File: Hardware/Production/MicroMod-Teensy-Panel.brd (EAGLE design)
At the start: 177.1 x 83.1 mm, 986 parts, among them J1 MICROMOD-2222, J10 MICROMOD-2222, J11 MICROMOD-2222, J12 MICROMOD-2222, J13 MICROMOD-2222, J14 MICROMOD-2222, J2 MICROMOD-2222, J3 MICROMOD-2222, J4 MICROMOD-2222, J5 MICROMOD-2222, J6 MICROMOD-2222, J7 MICROMOD-2222, J8 MICROMOD-2222, J9 MICROMOD-2222, U1 IMXRT1062DV10X10, U10 IMXRT1062DV10X10, U11 W25QXX, U12 MKL02Z32VFG4, U13 IMXRT1062DV10X10, U14 W25QXX, U15 MKL02Z32VFG4, U16 IMXRT1062DV10X10, U17 W25QXX, U18 MKL02Z32VFG4, U19 IMXRT1062DV10X10, U2 W25QXX, U20 W25QXX, U21 MKL02Z32VFG4, U22 IMXRT1062DV10X10, U23 W25QXX, U24 MKL02Z32VFG4, U25 IMXRT1062DV10X10, U26 W25QXX, U27 MKL02Z32VFG4, U28 IMXRT1062DV10X10, U29 W25QXX, U3 MKL02Z32VFG4, U30 MKL02Z32VFG4, U31 IMXRT1062DV10X10, U32 W25QXX, U33 MKL02Z32VFG4, U34 IMXRT1062DV10X10, U35 W25QXX, U36 MKL02Z32VFG4, U37 IMXRT1062DV10X10, U38 W25QXX, U39 MKL02Z32VFG4, U4 IMXRT1062DV10X10, U40 IMXRT1062DV10X10, U41 W25QXX, U42 MKL02Z32VFG4, U5 W25QXX, U6 MKL02Z32VFG4, U7 IMXRT1062DV10X10, U8 W25QXX, U9 MKL02Z32VFG4, Y1 32.768kHz, Y10 24MHz, Y11 32.768kHz, Y12 24MHz, Y13 32.768kHz, Y14 24MHz, Y15 32.768kHz, Y16 24MHz, Y17 32.768kHz, Y18 24MHz, Y19 32.768kHz, Y2 24MHz, Y20 24MHz, Y21 32.768kHz, Y22 24MHz, Y23 32.768kHz, Y24 24MHz, Y25 32.768kHz, Y26 24MHz, Y27 32.768kHz, Y28 24MHz, Y3 32.768kHz, Y4 24MHz, Y5 32.768kHz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

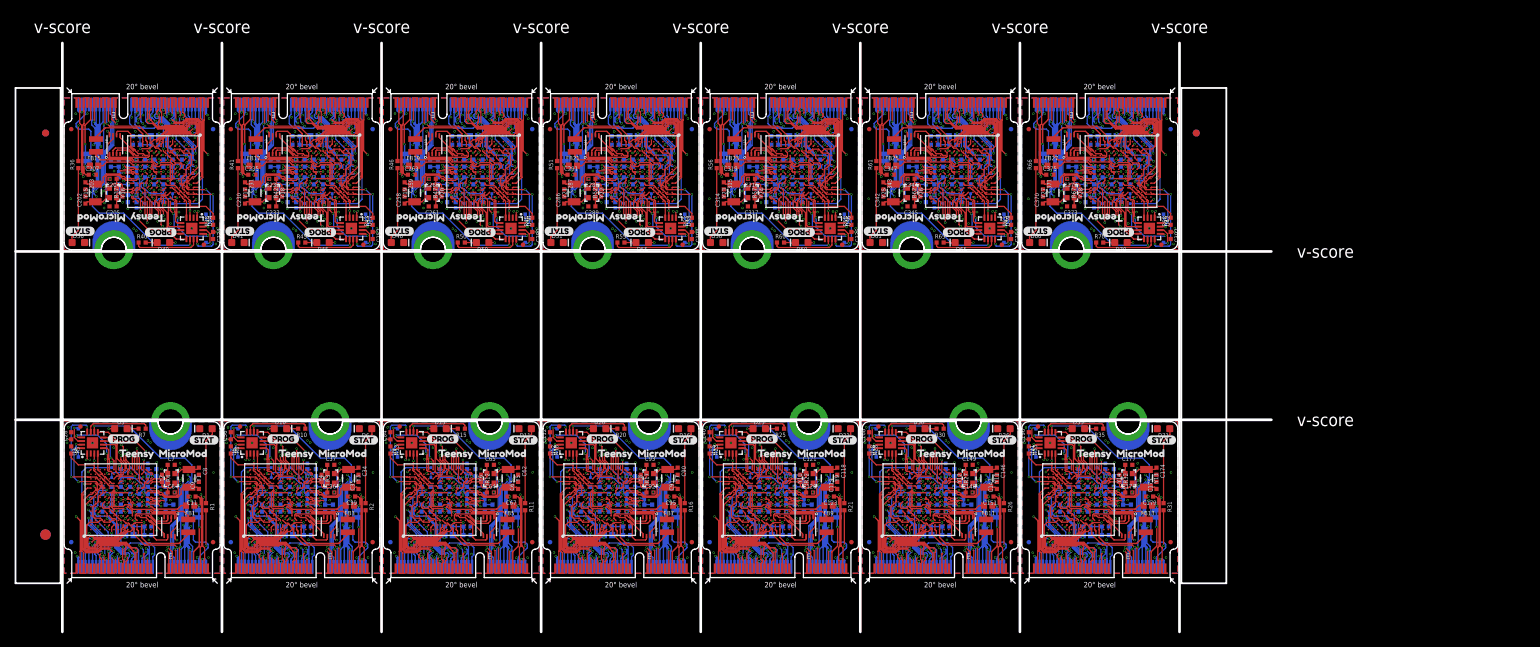
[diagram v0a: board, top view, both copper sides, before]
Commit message: Routed with 5mil. Increased clk spacing.
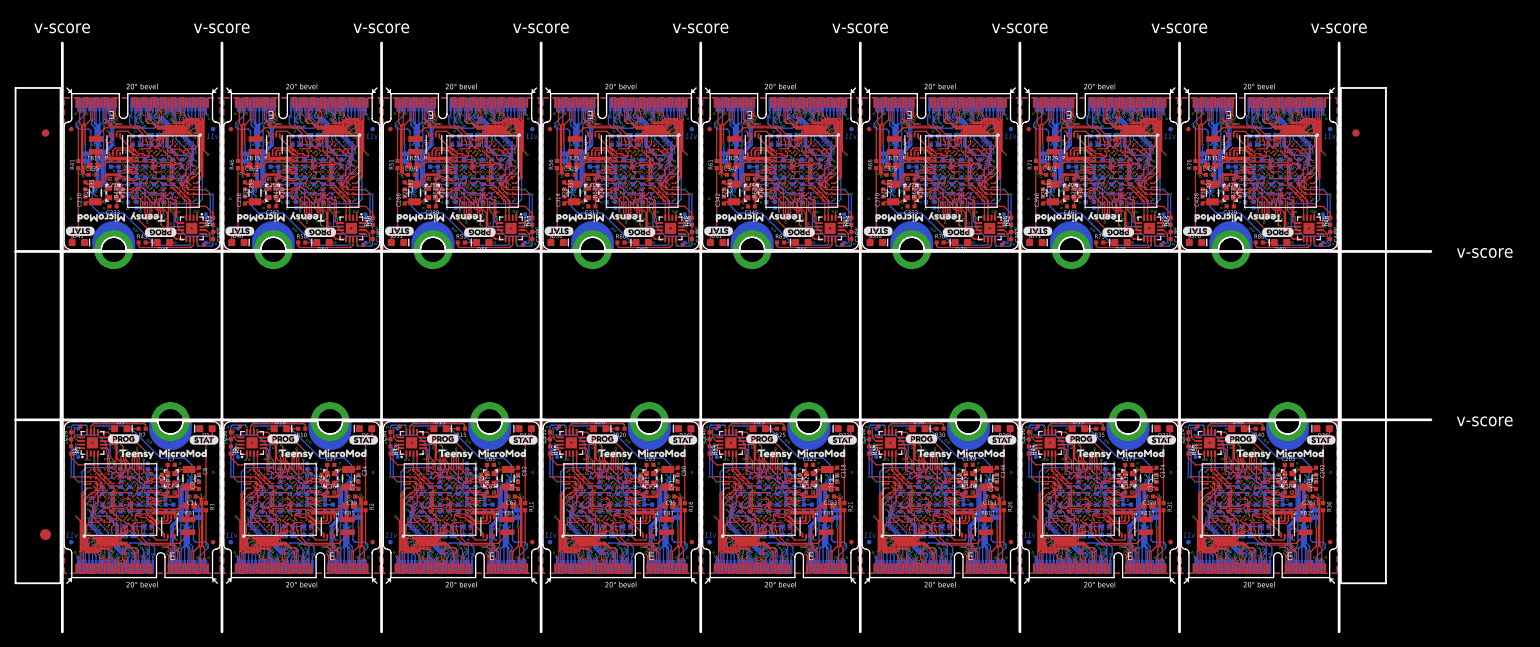
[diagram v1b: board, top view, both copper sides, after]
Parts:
- added C393, C403, C421, C431: 2.2uF, SparkFun-Capacitors:0402-TIGHT
- added C394, C406, C410, C418, C419, C422, C434, C438, C446, C447: 4.7uF, SparkFun-Capacitors:0402-TIGHT
- added C395, C396, C404, C405, C407, C409, C412, C414, C415, C416, C417, C420, C423, C424, C432, C433, C435, C437, C440, C442, C443, C444, C445, C448: 0.22uF, SparkFun-Capacitors:0402-TIGHT
- added C397, C408, C425, C436: 10nF, SparkFun-Capacitors:0402-TIGHT
- added C398, C399, C426, C427: 20pF, SparkFun-Capacitors:0402-TIGHT
- added C400, C401, C428, C429: 12pF, SparkFun-Capacitors:0402-TIGHT
- added C402, C411, C413, C430, C439, C441: 10uF, SparkFun-Capacitors:0402-TIGHT
- added D71, D76: BLUE, SparkFun-LED:LED-0603
- added D72, D77: 120mA370mV, SparkFun-DiscreteSemi:SOD-523
- added D73, D74, D78, D79: 120mA/370mV, SparkFun-DiscreteSemi:SOD-523
- added D75, D80: Yellow, SparkFun-LED:LED-0603
- added FB29, FB30, FB31, FB32: 120Ω, SparkFun-Coils:0402
- added FD57, FD58, FD59, FD60, FD61, FD62, FD63, FD64: FIDUCIALUFIDUCIAL, SparkFun-Aesthetics:FIDUCIAL-MICRO
- added J15, J16: MICROMOD-2222, Teensy:M.2-CARD-E-22
- added L15, L16: 4.7μH, SparkFun-Coils:1008(2520)
- added LOGO15, LOGO16: SFE_LOGO_NAME_FLAME.1_INCH, SparkFun-Aesthetics:SFE_LOGO_NAME_FLAME_.1
- added MEAS14, MEAS15: JUMPER-SMT_2_NC_TRACE_SILK, SparkFun-Jumpers:SMT-JUMPER_2_NC_TRACE_SILK
- added R71, R75, R76, R80: 1k, SparkFun-Resistors:0402-TIGHT
- added R72, R77: 2.2M, SparkFun-Resistors:0402-TIGHT
- added R73, R74, R78, R79: 100k, SparkFun-Resistors:0402-TIGHT
- added TP141, TP151: 32kHz Test, SparkFun-Connectors:PAD.02X.02
- added TP142, TP143, TP144, TP145, TP146, TP147, TP148, TP149, TP150, TP152, TP153, TP154, TP155, TP156, TP157, TP158, TP159, TP160: (no value), SparkFun-Connectors:PAD.02X.02
- added U$100, U$103, U$107, U$110: (no value), buzzard_labels (1):TEENSY2
- added U$101, U$108: (no value), SparkFun-Buzzard:STAT_32
- added U$102, U$109: (no value), SparkFun-Buzzard:PROG_32
- added U$104, U$106, U$111, U$99: (no value), buzzard_labels (1):MICROMOD0
- added U$105, U$112: (no value), SparkFun-Buzzard:MEAS_32
- added U43, U46: IMXRT1062DV10X10, Teensy:IMXRT1062
- added U44, U47: W25QXX3X2, Teensy:USON-8
- added U45, U48: MKL02Z32VFG4, Teensy:QFN-16
- added Y29, Y31: 32.768kHz, SparkFun-Clocks:CRYSTAL-SMD-3.2X1.5MM
- added Y30, Y32: 24MHz, SparkFun-Clocks:CRYSTAL-SMD-2.0X1.6MM
- MEAS, MEAS1, MEAS10, MEAS11, MEAS12, MEAS13, MEAS2, MEAS3, MEAS4, MEAS5, MEAS6, MEAS7, MEAS8, MEAS9: value (none) -> JUMPER-SMT_2_NC_TRACE_SILK
- U11, U14, U17, U2, U20, U23, U26, U29, U32, U35, U38, U41, U5, U8: value W25QXX -> W25QXX3X2
- moved FD29 186.9 mm to (178.6, 5.80), turned to 0 degrees
- moved U$56 186.1 mm to (178.7, 7.40), turned to 90 degrees
- moved U$55 182.6 mm to (179.2, 16.3), turned to 0 degrees
- moved R36 182.1 mm to (177.6, 10.8), turned to 270 degrees
- moved MEAS7 180.7 mm to (176.6, 9.80), turned to 90 degrees
- moved U$54 179.8 mm to (178.1, 17.9), turned to 0 degrees
- moved FD32 179.5 mm to (178.6, 21.8), turned to 0 degrees
- moved L8 178.8 mm to (175.1, 8.10), turned to 90 degrees
- moved C203 178.6 mm to (176.6, 13.8), turned to 90 degrees
- moved C202 177.7 mm to (176.6, 15.8), turned to 270 degrees
- moved FB15 177.7 mm to (175.3, 11.0), turned to 180 degrees
- moved C207 177.5 mm to (175.6, 12.2), turned to 180 degrees
- moved D36 177.5 mm to (177.6, 21.8), turned to 180 degrees
- moved Y15 175.4 mm to (175.2, 14.8), turned to 270 degrees
- moved U23 173.8 mm to (172.4, 7.99), turned to 270 degrees
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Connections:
- net ADC1ST/14/A0 renamed A0/14
- net ADC1ST/14/A1 renamed A0/1
- net ADC1ST/14/A10 renamed A0/10
- net ADC1ST/14/A11 renamed A0/11
- net ADC1ST/14/A12 renamed A0/12
- net ADC1ST/14/A13 renamed A0/13
- net ADC1ST/14/A2 renamed A0/2
- net ADC1ST/14/A3 renamed A0/3
- net ADC1ST/14/A4 renamed A0/4
- net ADC1ST/14/A5 renamed A0/5
- net ADC1ST/14/A6 renamed A0/6
- net ADC1ST/14/A7 renamed A0/7
- net ADC1ST/14/A8 renamed A0/8
- net ADC1ST/14/A9 renamed A0/9
- net ADC2ND/15/A1 renamed A1/15
- net ADC2ND/15/A10 renamed A1/9
- net ADC2ND/15/A11 renamed A1/10
- net ADC2ND/15/A12 renamed A1/11
- net ADC2ND/15/A13 renamed A1/12
- net ADC2ND/15/A14 renamed A1/13
- net ADC2ND/15/A2 renamed A1/1
- net ADC2ND/15/A3 renamed A1/2
- net ADC2ND/15/A4 renamed A1/3
- net ADC2ND/15/A5 renamed A1/4
- net ADC2ND/15/A6 renamed A1/5
- net ADC2ND/15/A7 renamed A1/6
- net ADC2ND/15/A8 renamed A1/7
- net ADC2ND/15/A9 renamed A1/8
- net GPIO_1ST/1 renamed D0/1
- net GPIO_1ST/10 renamed D0/10
- net GPIO_1ST/11 renamed D0/11
- net GPIO_1ST/12 renamed D0/12
- net GPIO_1ST/13 renamed D0/13
- net GPIO_1ST/14 renamed D0/14
- net GPIO_1ST/2 renamed D0/2
- net GPIO_1ST/3 renamed D0/3
- net GPIO_1ST/4 renamed D0/4
- net GPIO_1ST/5 renamed D0/5
- net GPIO_1ST/6 renamed D0/6
- net GPIO_1ST/7 renamed D0/7
- net GPIO_1ST/8 renamed D0/8
- net GPIO_1ST/9 renamed D0/9
- net GPIO_2ND/1 renamed D1/1
- net GPIO_2ND/10 renamed D1/10
- net GPIO_2ND/11 renamed D1/11
- net GPIO_2ND/12 renamed D1/12
- net GPIO_2ND/13 renamed D1/13
- net GPIO_2ND/14 renamed D1/14
- net GPIO_2ND/2 renamed D1/2
- net GPIO_2ND/3 renamed D1/3
- net GPIO_2ND/4 renamed D1/4
- net GPIO_2ND/5 renamed D1/5
- net GPIO_2ND/6 renamed D1/6
- net GPIO_2ND/7 renamed D1/7
- net GPIO_2ND/8 renamed D1/8
- net GPIO_2ND/9 renamed D1/9
- net PWM_1ST/1 renamed PWM0/1
- net PWM_1ST/10 renamed PWM0/10
- net PWM_1ST/11 renamed PWM0/11
- net PWM_1ST/12 renamed PWM0/12
- net PWM_1ST/13 renamed PWM0/13
- net PWM_1ST/14 renamed PWM0/14
- net PWM_1ST/2 renamed PWM0/2
- net PWM_1ST/3 renamed PWM0/3
- net PWM_1ST/4 renamed PWM0/4
- net PWM_1ST/5 renamed PWM0/5
- net PWM_1ST/6 renamed PWM0/6
- net PWM_1ST/7 renamed PWM0/7
- net PWM_1ST/8 renamed PWM0/8
- net PWM_1ST/9 renamed PWM0/9
- net PWM_2ND/1 renamed PWM1/1
- net PWM_2ND/10 renamed PWM1/10
- net PWM_2ND/11 renamed PWM1/11
- net PWM_2ND/12 renamed PWM1/12
- net PWM_2ND/13 renamed PWM1/13
- net PWM_2ND/14 renamed PWM1/14
- net PWM_2ND/2 renamed PWM1/2
- net PWM_2ND/3 renamed PWM1/3
- net PWM_2ND/4 renamed PWM1/4
- net PWM_2ND/5 renamed PWM1/5
- net PWM_2ND/6 renamed PWM1/6
- net PWM_2ND/7 renamed PWM1/7
- net PWM_2ND/8 renamed PWM1/8
- net PWM_2ND/9 renamed PWM1/9
- net SCL2/24/A1 renamed SCL1/24/A1
- net SCL2/24/A10 renamed SCL1/24/A10
- net SCL2/24/A11 renamed SCL1/24/A11
- net SCL2/24/A12 renamed SCL1/24/A12
- net SCL2/24/A13 renamed SCL1/24/A13
- net SCL2/24/A14 renamed SCL1/24/A14
- net SCL2/24/A2 renamed SCL1/24/A2
- net SCL2/24/A3 renamed SCL1/24/A3
- net SCL2/24/A4 renamed SCL1/24/A4
- net SCL2/24/A5 renamed SCL1/24/A5
- net SCL2/24/A6 renamed SCL1/24/A6
- net SCL2/24/A7 renamed SCL1/24/A7
- net SCL2/24/A8 renamed SCL1/24/A8
- net SCL2/24/A9 renamed SCL1/24/A9
- net SDA2/25/A1 renamed SDA1/25/A1
- net SDA2/25/A10 renamed SDA1/25/A10
- net SDA2/25/A11 renamed SDA1/25/A11
- net SDA2/25/A12 renamed SDA1/25/A12
- net SDA2/25/A13 renamed SDA1/25/A13
- net SDA2/25/A14 renamed SDA1/25/A14
- net SDA2/25/A2 renamed SDA1/25/A2
- net SDA2/25/A3 renamed SDA1/25/A3
- net SDA2/25/A4 renamed SDA1/25/A4
- net SDA2/25/A5 renamed SDA1/25/A5
- net SDA2/25/A6 renamed SDA1/25/A6
- net SDA2/25/A7 renamed SDA1/25/A7
- net SDA2/25/A8 renamed SDA1/25/A8
- net SDA2/25/A9 renamed SDA1/25/A9
- new net 3.3V14: C393.1, C394.1, C395.1, C396.1, C397.1, C420.1, D72.A, D75.A, FB30.1, J15.2, J15.4, J15.74, R74.1, U43.E6, U43.E9, U43.F10, U43.F5, U43.J10, U43.J6, U43.K4, U43.K5, U43.N14, U43.P12, U44.8, U45.1
- new net 3.3V15: C421.1, C422.1, C423.1, C424.1, C425.1, C448.1, D77.A, D80.A, FB32.1, J16.2, J16.4, J16.74, R79.1, U46.E6, U46.E9, U46.F10, U46.F5, U46.J10, U46.J6, U46.K4, U46.K5, U46.N14, U46.P12, U47.8, U48.1
- new net 34/DAT15: J15.66, U43.K1
- new net 34/DAT16: J16.66, U46.K1
- new net 35/DAT14: J15.64, U43.J1
- new net 35/DAT15: J16.64, U46.J1
- new net 36/CLK14: J15.60, U43.J3
- new net 36/CLK15: J16.60, U46.J3
- new net 37/CMD14: J15.62, U43.J4
- new net 37/CMD15: J16.62, U46.J4
- new net 38/DAT15: J15.70, U43.H2
- new net 38/DAT16: J16.70, U46.H2
- new net 39/DAT15: J15.68, U43.J2
- new net 39/DAT16: J16.68, U46.J2
- new net A0/15: J15.34, U43.L11
- new net A0/16: J16.34, U46.L11
- new net A1/14: J15.38, U43.M12
- new net A1/16: J16.38, U46.M12
- new net AUD_IN/15: J15.54, U43.A11
- new net AUD_IN/16: J16.54, U46.A11
- new net AUD_OUT/15: J15.56, U43.B11
- new net AUD_OUT/16: J16.56, U46.B11
- new net BATT_VIN/22/A15: J15.51, U43.H13
- new net BATT_VIN/22/A16: J16.51, U46.H13
- new net BCLK/21/A15: J15.50, U43.J13
- new net BCLK/21/A16: J16.50, U46.J13
- new net BOOTMODE14: U43.F11, U45.4
- new net BOOTMODE15: U46.F11, U48.4
- new net CAN_RX/14: J15.41, U43.E4
- new net CAN_RX/15: J16.41, U46.E4
- new net CAN_TX/14: J15.43, U43.C3
- new net CAN_TX/15: J16.43, U46.C3
- new net CS/15: J15.49, U43.D7
- new net CS/16: J16.49, U46.D7
- new net D0/15: J15.10, U43.H5
- new net D0/16: J16.10, U46.H5
- new net D1/15: J15.18, U43.H3
- new net D1/16: J16.18, U46.H3
- new net DEBUG_EN14: U43.F3, U45.15
- new net DEBUG_EN15: U46.F3, U48.15
- new net DEBUG_SWO14: U43.D10, U45.12
- new net DEBUG_SWO15: U46.D10, U48.12
- new net GND14: C393.2, C394.2, C395.2, C396.2, C397.2, C398.2, C399.2, C400.2, C401.2, C402.2, C403.2, C404.2, C405.2, C406.2, C407.2, C408.2, C409.2, C410.2, C411.2, C412.2, C413.2, C414.2, C415.2, C416.2, C417.2, C418.2, C419.2, C420.2, D71.C, J15.1, J15.33, J15.36, J15.39, J15.45, J15.7, J15.75, J15.GND, J15.GND-SM-B, R72.1, R73.1, U43.A1, U43.A14, U43.B10, U43.B5, U43.E13, U43.E2, U43.G14, U43.G7, U43.G8, U43.H7, U43.H8, U43.J7, U43.J8, U43.K13, U43.K2, U43.K6, U43.K9, U43.L9, U43.N1, U43.N2, U43.N5, U43.N8, U43.P1, U43.P14, U44.4, U45.17, U45.2
- new net GND15: C421.2, C422.2, C423.2, C424.2, C425.2, C426.2, C427.2, C428.2, C429.2, C430.2, C431.2, C432.2, C433.2, C434.2, C435.2, C436.2, C437.2, C438.2, C439.2, C440.2, C441.2, C442.2, C443.2, C444.2, C445.2, C446.2, C447.2, C448.2, D76.C, J16.1, J16.33, J16.36, J16.39, J16.45, J16.7, J16.75, J16.GND, J16.GND-SM-B, R77.1, R78.1, U46.A1, U46.A14, U46.B10, U46.B5, U46.E13, U46.E2, U46.G14, U46.G7, U46.G8, U46.H7, U46.H8, U46.J7, U46.J8, U46.K13, U46.K2, U46.K6, U46.K9, U46.L9, U46.N1, U46.N2, U46.N5, U46.N8, U46.P1, U46.P14, U47.4, U48.17, U48.2
- new net GPIO/26/A15: J15.42, U43.G12
- new net GPIO/26/A16: J16.42, U46.G12
- new net GPIO/27/A15: J15.44, U43.J14
- new net GPIO/27/A16: J16.44, U46.J14
- new net GPIO/71: J15.71, U43.A10
- new net GPIO/72: J15.40, U43.D9
- new net GPIO/73: J15.46, U43.D5
- new net GPIO/74: J15.48, U43.C10
- new net GPIO/75: J15.73, U43.H4
- new net GPIO/76: J16.71, U46.A10
- new net GPIO/77: J16.40, U46.D9
- new net GPIO/78: J16.46, U46.D5
- new net GPIO/79: J16.48, U46.C10
- new net GPIO/80: J16.73, U46.H4
- new net I2C_!INT!/14: J15.16, U43.C5
- new net I2C_!INT!/15: J16.16, U46.C5
- new net JTAG_MOD14: U43.F13, U45.13
- new net JTAG_MOD15: U46.F13, U48.13
- new net JTAG_TCK14: U43.F12, U45.8
- new net JTAG_TCK15: U46.F12, U48.8
- new net JTAG_TDI14: U43.F14, U45.7
- new net JTAG_TDI15: U46.F14, U48.7
- new net JTAG_TDO14: U43.G13, U45.6
- new net JTAG_TDO15: U46.G13, U48.6
- new net JTAG_TMS14: U43.E14, U45.5
- new net JTAG_TMS15: U46.E14, U48.5
- new net JTAG_TRST14: R73.2, U43.G10, U43.K3, U45.3
- new net JTAG_TRST15: R78.2, U46.G10, U46.K3, U48.3
- new net LRCLK/20/A15: J15.52, U43.L13
- new net LRCLK/20/A16: J16.52, U46.L13
- new net MCLK/23/A15: J15.58, U43.M13
- new net MCLK/23/A16: J16.58, U46.M13
- new net MISO/15: J15.61, U43.E7
- new net MISO/16: J16.61, U46.E7
- new net MOSI/15: J15.59, U43.E8
- new net MOSI/16: J16.59, U46.E8
- new net N$197: C399.1, U43.P9, Y29.P$2
- new net N$198: C398.1, U43.N9, Y29.P$1
- new net N$199: TP141.P$1, U43.M14
- new net N$200: D71.A, R71.1
- new net N$201: C401.1, U43.N11, Y30.3
- new net N$202: C400.1, R72.2, U43.P11, Y30.1
- new net N$203: C402.1, C406.1, C407.1, FB30.2, U43.L1, U43.L2
- new net N$204: L15.1, U43.M1, U43.M2
- new net N$205: C415.1, TP144.P$1, U43.M10
- new net N$206: C416.1, C418.1, TP145.P$1, U43.P10
- new net N$207: C417.1, C419.1, TP146.P$1, U43.P8
- new net N$208: R75.1, U45.11
- new net N$209: D75.C, R75.2
- new net N$210: C403.1, FB29.1, MEAS14.2
- new net N$211: C427.1, U46.P9, Y31.P$2
- new net N$212: C426.1, U46.N9, Y31.P$1
- new net N$213: TP151.P$1, U46.M14
- new net N$214: D76.A, R76.1
- new net N$215: C429.1, U46.N11, Y32.3
- new net N$216: C428.1, R77.2, U46.P11, Y32.1
- new net N$217: C430.1, C434.1, C435.1, FB32.2, U46.L1, U46.L2
- new net N$218: L16.1, U46.M1, U46.M2
- new net N$219: C443.1, TP154.P$1, U46.M10
- new net N$220: C444.1, C446.1, TP155.P$1, U46.P10
- new net N$221: C445.1, C447.1, TP156.P$1, U46.P8
- new net N$222: R80.1, U48.11
- new net N$223: D80.C, R80.2
- new net N$224: C431.1, FB31.1, MEAS15.2
- new net ON/!OFF!14: J15.6, U43.M6
- new net ON/!OFF!15: J16.6, U46.M6
- new net PMIC14: R74.2, U43.K7
- new net PMIC15: R79.2, U46.K7
- new net PORB_RESET14: U43.M7, U45.9
- new net PORB_RESET15: U46.M7, U48.9
- new net PROGRAM14: J15.11, U45.10
- new net PROGRAM15: J16.11, U48.10
- new net PWM0/15: J15.32, U43.G5
- new net PWM0/16: J16.32, U46.G5
- new net PWM1/15: J15.47, U43.F2
- new net PWM1/16: J16.47, U46.F2
- new net QSPI-CLK14: U43.L4, U44.6
- new net QSPI-CLK15: U46.L4, U47.6
- new net QSPI-CS14: U43.L3, U44.1
- new net QSPI-CS15: U46.L3, U47.1
- new net QSPI56: U43.P3, U44.5
- new net QSPI57: U43.N4, U44.2
- new net QSPI58: U43.P4, U44.3
- new net QSPI59: U43.P5, U44.7
- new net QSPI60: U46.P3, U47.5
- new net QSPI61: U46.N4, U47.2
- new net QSPI62: U46.P4, U47.3
- new net QSPI63: U46.P5, U47.7
- new net RX0/14: J15.19, U43.G11
- new net RX0/15: J16.19, U46.G11
- new net RX1/16/A15: J15.20, U43.K10
- new net RX1/16/A16: J16.20, U46.K10
- new net SCK/15: J15.57, R71.2, U43.D8
- new net SCK/16: J16.57, R76.2, U46.D8
- new net SCL/19/A15: J15.14, U43.J11
- new net SCL/19/A16: J16.14, U46.J11
- new net SCL1/24/A15: J15.55, U43.K14
- new net SCL1/24/A16: J16.55, U46.K14
- new net SDA/18/A15: J15.12, U43.K11
- new net SDA/18/A16: J16.12, U46.K11
- new net SDA1/25/A15: J15.53, U43.L14
- new net SDA1/25/A16: J16.53, U46.L14
- new net SWD_CLK14: J15.21, TP148.P$1, U45.14
- new net SWD_CLK15: J16.21, TP158.P$1, U48.14
- new net SWD_DIO14: J15.23, TP147.P$1, U45.16
- new net SWD_DIO15: J16.23, TP157.P$1, U48.16
- new net TX0/15: J15.17, U43.M11
- new net TX0/16: J16.17, U46.M11
- new net TX1/17/A15: J15.22, U43.J12
- new net TX1/17/A16: J16.22, U46.J12
- new net USB2_D+14: J15.35, U43.P7
- new net USB2_D+15: J16.35, U46.P7
- new net USB2_D-14: J15.37, U43.N7
- new net USB2_D-15: J16.37, U46.N7
- new net USB_D+14: J15.3, U43.L8
- new net USB_D+15: J16.3, U46.L8
- new net USB_D-14: J15.5, U43.M8
- new net USB_D-15: J16.5, U46.M8
- new net VCC14: C404.1, C405.1, FB29.2, TP142.P$1, U43.N6, U43.P6
- new net VCC15: C432.1, C433.1, FB31.2, TP152.P$1, U46.N6, U46.P6
- new net VDD_SOC_IN14: C408.1, C409.1, C410.1, C411.1, L15.2, TP149.P$1, U43.F6, U43.F7, U43.F8, U43.F9, U43.G6, U43.G9, U43.H6, U43.H9, U43.J5, U43.J9
- new net VDD_SOC_IN15: C436.1, C437.1, C438.1, C439.1, L16.2, TP159.P$1, U46.F6, U46.F7, U46.F8, U46.F9, U46.G6, U46.G9, U46.H6, U46.H9, U46.J5, U46.J9
- new net VDD_USB_CAP14: C412.1, C413.1, D74.A, TP150.P$1, U43.K8
- new net VDD_USB_CAP15: C440.1, C441.1, D79.A, TP160.P$1, U46.K8
- new net VSS_SNVS_IN14: C414.1, D72.C, D73.C, D74.C, TP143.P$1, U43.M9
- new net VSS_SNVS_IN15: C442.1, D77.C, D78.C, D79.C, TP153.P$1, U46.M9
- new net V_BATT14: D73.A, J15.72
- new net V_BATT15: D78.A, J16.72
- new net V_USB14: J15.9, MEAS14.1
- new net V_USB15: J16.9, MEAS15.1
- net RX0/0: now also J1.19; no longer J1.20
- net RX0/1: now also J2.19; no longer J2.20
- net RX0/10: now also J11.19; no longer J11.20
- net RX0/11: now also J12.19; no longer J12.20
- net RX0/12: now also J13.19; no longer J13.20
- net RX0/13: now also J14.19; no longer J14.20
- net RX0/2: now also J3.19; no longer J3.20
- net RX0/3: now also J4.19; no longer J4.20
- net RX0/4: now also J5.19; no longer J5.20
- net RX0/5: now also J6.19; no longer J6.20
- net RX0/6: now also J7.19; no longer J7.20
- net RX0/7: now also J8.19; no longer J8.20
- net RX0/8: now also J9.19; no longer J9.20
- net RX0/9: now also J10.19; no longer J10.20
- net RX1/16/A1: now also J2.20; no longer J2.19
- net RX1/16/A10: now also J10.20; no longer J10.19
- net RX1/16/A11: now also J11.20; no longer J11.19
- net RX1/16/A12: now also J12.20; no longer J12.19
- net RX1/16/A13: now also J13.20; no longer J13.19
- net RX1/16/A14: now also J14.20; no longer J14.19
- net RX1/16/A2: now also J1.20; no longer J1.19
- net RX1/16/A3: now also J3.20; no longer J3.19
- net RX1/16/A4: now also J4.20; no longer J4.19
- net RX1/16/A5: now also J5.20; no longer J5.19
- net RX1/16/A6: now also J6.20; no longer J6.19
- net RX1/16/A7: now also J7.20; no longer J7.19
- net RX1/16/A8: now also J8.20; no longer J8.19
- net RX1/16/A9: now also J9.20; no longer J9.19
- net TX0/1: now also J1.17; no longer J1.22
- net TX0/10: now also J10.17; no longer J10.22
- net TX0/11: now also J11.17; no longer J11.22
- net TX0/12: now also J12.17; no longer J12.22
- net TX0/13: now also J13.17; no longer J13.22
- net TX0/14: now also J14.17; no longer J14.22
- net TX0/2: now also J2.17; no longer J2.22
- net TX0/3: now also J3.17; no longer J3.22
- net TX0/4: now also J4.17; no longer J4.22
- net TX0/5: now also J5.17; no longer J5.22
- net TX0/6: now also J6.17; no longer J6.22
- net TX0/7: now also J7.17; no longer J7.22
- net TX0/8: now also J8.17; no longer J8.22
- net TX0/9: now also J9.17; no longer J9.22
- net TX1/17/A1: now also J2.22; no longer J2.17
- net TX1/17/A10: now also J10.22; no longer J10.17
- net TX1/17/A11: now also J11.22; no longer J11.17
- net TX1/17/A12: now also J12.22; no longer J12.17
- net TX1/17/A13: now also J13.22; no longer J13.17
- net TX1/17/A14: now also J14.22; no longer J14.17
- net TX1/17/A2: now also J3.22; no longer J3.17
- net TX1/17/A3: now also J1.22; no longer J1.17
- net TX1/17/A4: now also J4.22; no longer J4.17
- net TX1/17/A5: now also J5.22; no longer J5.17
- net TX1/17/A6: now also J6.22; no longer J6.17
- net TX1/17/A7: now also J7.22; no longer J7.17
- net TX1/17/A8: now also J8.22; no longer J8.17
- net TX1/17/A9: now also J9.22; no longer J9.17
- net VDD_SOC_IN: now also U1.J5
- net VDD_SOC_IN1: now also U4.J5
- net VDD_SOC_IN10: now also U31.J5
- net VDD_SOC_IN11: now also U34.J5
- net VDD_SOC_IN12: now also U37.J5
- net VDD_SOC_IN13: now also U40.J5
- net VDD_SOC_IN2: now also U7.J5
- net VDD_SOC_IN3: now also U10.J5
- net VDD_SOC_IN4: now also U13.J5
- net VDD_SOC_IN5: now also U16.J5
- net VDD_SOC_IN6: now also U19.J5
- net VDD_SOC_IN7: now also U22.J5
- net VDD_SOC_IN8: now also U25.J5
- net VDD_SOC_IN9: now also U28.J5
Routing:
- net SWD_CLK15: track 0.00 -> 34.9 mm, vias 0 -> 3
- net SWD_CLK14: track 0.00 -> 34.9 mm, vias 0 -> 3
- net SCK/16: track 0.00 -> 34.8 mm, vias 0 -> 4
- net SCK/15: track 0.00 -> 34.8 mm, vias 0 -> 4
- net PROGRAM15: track 0.00 -> 32.0 mm, vias 0 -> 2
- net PROGRAM14: track 0.00 -> 32.0 mm, vias 0 -> 2
- net SWD_DIO15: track 0.00 -> 31.8 mm, vias 0 -> 3
- net SWD_DIO14: track 0.00 -> 31.8 mm, vias 0 -> 3
- net A0/16: track 0.00 -> 29.0 mm, vias 0 -> 2
- net A0/15: track 0.00 -> 29.0 mm, vias 0 -> 2
- net JTAG_TRST15: track 0.00 -> 28.2 mm, vias 0 -> 3
- net JTAG_TRST14: track 0.00 -> 28.2 mm, vias 0 -> 3
- net TX0/16: track 0.00 -> 28.1 mm, vias 0 -> 3
- net TX0/15: track 0.00 -> 28.1 mm, vias 0 -> 3
- net 3.3V15: track 0.00 -> 26.0 mm, vias 0 -> 12
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- added copper zone on layer 2, net 3.3V14
- added copper zone on layer 2, net 3.3V15
- added copper zone on layer 1, net GND14
- added copper zone on layer 15, net GND14
- added copper zone on layer 16, net GND14
- added copper zone on layer 1, net GND15
- added copper zone on layer 15, net GND15
- added copper zone on layer 16, net GND15
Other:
- board size 177.1 x 83.1 mm -> 199.6 x 83.1 mm
- board text added: "v11"

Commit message: Breakout PMIC. Reduce beads to 0402T.
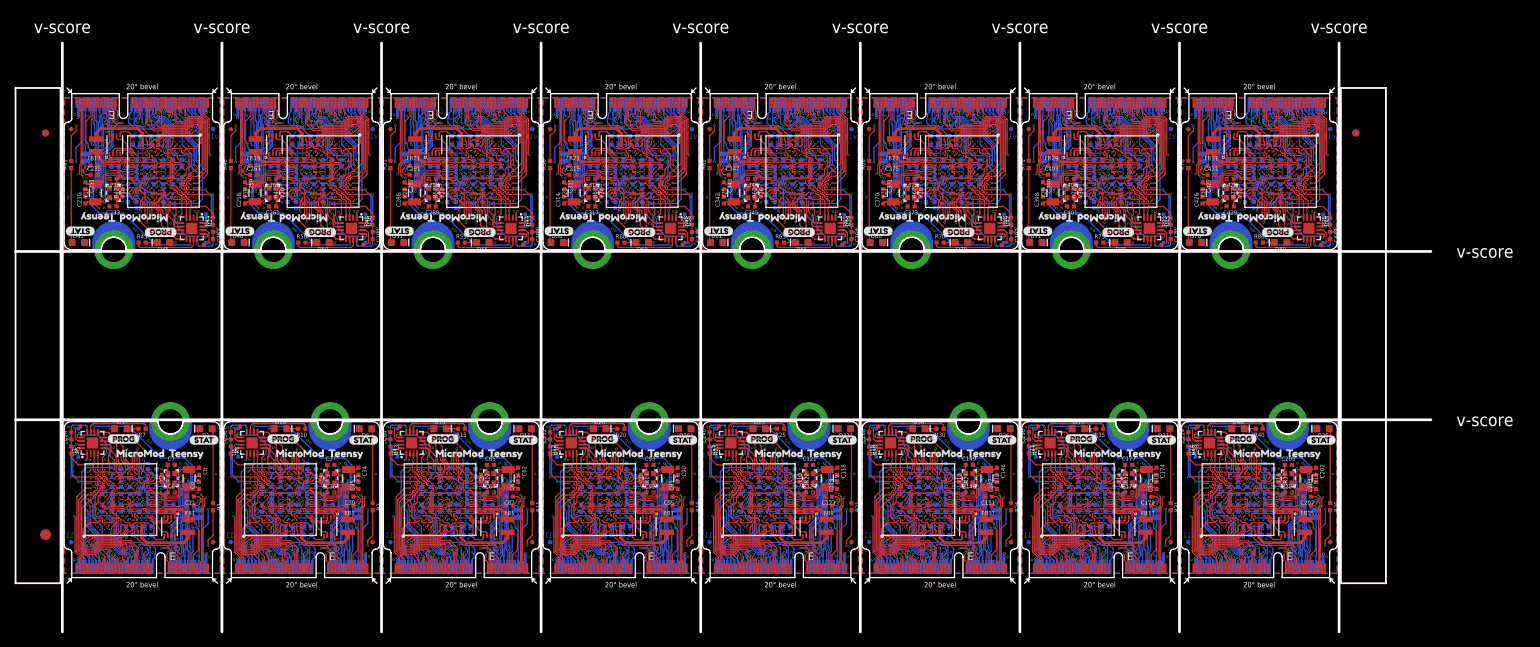
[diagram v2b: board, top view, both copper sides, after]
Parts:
- added TP161, TP162, TP163, TP164, TP165, TP167, TP168, TP169, TP170, TP171, TP172, TP173, TP174, TP175, TP176: (no value), SparkFun-Connectors:PAD.02X.02
- added TP166: 32kHz Test, SparkFun-Connectors:PAD.02X.02
- FB1, FB10, FB11, FB12, FB13, FB14, FB15, FB16, FB17, FB18, FB19, FB2, FB20, FB21, FB22, FB23, FB24, FB25, FB26, FB27, FB28, FB29, FB3, FB30, FB31, FB32, FB4, FB5, FB6, FB7, FB8, FB9: device SparkFun-Coils:0402 -> SparkFun-Coils:0402-TIGHT
- MEAS, MEAS1, MEAS10, MEAS11, MEAS12, MEAS13, MEAS14, MEAS15, MEAS2, MEAS3, MEAS4, MEAS5, MEAS6, MEAS7, MEAS8, MEAS9: value JUMPER-SMT_2_NC_TRACE_SILK -> (none)
- TP100, TP12, TP122, TP133, TP144, TP155, TP23, TP34, TP45, TP56, TP67, TP78, TP89: value (none) -> 32kHz Test
- TP101, TP121, TP131, TP141, TP151, TP2, TP21, TP31, TP41, TP51, TP61, TP71, TP81, TP91: value 32kHz Test -> (none)
- moved TP82 168.6 mm to (171.9, 14.3), turned to 0 degrees
- moved TP83 168.2 mm to (171.9, 11.8), turned to 0 degrees
- moved TP81 163.8 mm to (169.4, 14.3), turned to 0 degrees
- moved TP86 163.2 mm to (164.3, 11.8), turned to 270 degrees
- moved TP85 155.6 mm to (159.6, 21.8), turned to 0 degrees
- moved TP84 154.1 mm to (159.6, 17.8), turned to 0 degrees
- moved TP88 152.1 mm to (167.6, 11.1), turned to 0 degrees
- moved TP87 150.4 mm to (165.6, 14.3), turned to 270 degrees
- moved TP121 43.6 mm to (57.0, 58.7), turned to 180 degrees
- moved TP154 43.3 mm to (124.5, 58.7)
- moved TP143 43.2 mm to (102.0, 58.7)
- moved TP132 42.0 mm to (79.5, 58.7), turned to 180 degrees
- moved TP131 41.3 mm to (81.5, 55.5)
- moved TP153 41.3 mm to (126.5, 55.5), turned to 90 degrees
- moved TP141 40.2 mm to (105.3, 58.0)
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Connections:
- net VSS_SNVS_IN renamed VDD_SNVS_IN
- removed net VSS_SNVS_IN1: C50.1, D7.C, D8.C, D9.C, TP13.P$1, U4.M9
- removed net VSS_SNVS_IN10: C302.1, D52.C, D53.C, D54.C, TP103.P$1, U31.M9
- removed net VSS_SNVS_IN11: C330.1, D57.C, D58.C, D59.C, TP113.P$1, U34.M9
- removed net VSS_SNVS_IN12: C358.1, D62.C, D63.C, D64.C, TP123.P$1, U37.M9
- removed net VSS_SNVS_IN13: C386.1, D67.C, D68.C, D69.C, TP133.P$1, U40.M9
- removed net VSS_SNVS_IN14: C414.1, D72.C, D73.C, D74.C, TP143.P$1, U43.M9
- removed net VSS_SNVS_IN15: C442.1, D77.C, D78.C, D79.C, TP153.P$1, U46.M9
- removed net VSS_SNVS_IN2: C78.1, D12.C, D13.C, D14.C, TP23.P$1, U7.M9
- removed net VSS_SNVS_IN3: C106.1, D17.C, D18.C, D19.C, TP33.P$1, U10.M9
- removed net VSS_SNVS_IN4: C134.1, D22.C, D23.C, D24.C, TP43.P$1, U13.M9
- removed net VSS_SNVS_IN5: C162.1, D27.C, D28.C, D29.C, TP53.P$1, U16.M9
- removed net VSS_SNVS_IN6: C190.1, D32.C, D33.C, D34.C, TP63.P$1, U19.M9
- removed net VSS_SNVS_IN7: C218.1, D37.C, D38.C, D39.C, TP73.P$1, U22.M9
- removed net VSS_SNVS_IN8: C246.1, D42.C, D43.C, D44.C, TP83.P$1, U25.M9
- removed net VSS_SNVS_IN9: C274.1, D47.C, D48.C, D49.C, TP93.P$1, U28.M9
- new net VDD_SNVS_IN1: C50.1, D7.C, D8.C, D9.C, TP14.P$1, U4.M9
- new net VDD_SNVS_IN10: C302.1, D52.C, D53.C, D54.C, TP113.P$1, U31.M9
- new net VDD_SNVS_IN11: C330.1, D57.C, D58.C, D59.C, TP124.P$1, U34.M9
- new net VDD_SNVS_IN12: C358.1, D62.C, D63.C, D64.C, TP135.P$1, U37.M9
- new net VDD_SNVS_IN13: C386.1, D67.C, D68.C, D69.C, TP146.P$1, U40.M9
- new net VDD_SNVS_IN14: C414.1, D72.C, D73.C, D74.C, TP157.P$1, U43.M9
- new net VDD_SNVS_IN15: C442.1, D77.C, D78.C, D79.C, TP168.P$1, U46.M9
- new net VDD_SNVS_IN2: C78.1, D12.C, D13.C, D14.C, TP25.P$1, U7.M9
- new net VDD_SNVS_IN3: C106.1, D17.C, D18.C, D19.C, TP36.P$1, U10.M9
- new net VDD_SNVS_IN4: C134.1, D22.C, D23.C, D24.C, TP47.P$1, U13.M9
- new net VDD_SNVS_IN5: C162.1, D27.C, D28.C, D29.C, TP58.P$1, U16.M9
- new net VDD_SNVS_IN6: C190.1, D32.C, D33.C, D34.C, TP69.P$1, U19.M9
- new net VDD_SNVS_IN7: C218.1, D37.C, D38.C, D39.C, TP80.P$1, U22.M9
- new net VDD_SNVS_IN8: C246.1, D42.C, D43.C, D44.C, TP91.P$1, U25.M9
- new net VDD_SNVS_IN9: C274.1, D47.C, D48.C, D49.C, TP102.P$1, U28.M9
- net 3.3V: no longer J1.4
- net 3.3V1: no longer J2.4
- net 3.3V10: no longer J11.4
- net 3.3V11: no longer J12.4
- net 3.3V12: no longer J13.4
- net 3.3V13: no longer J14.4
- net 3.3V14: no longer J15.4
- net 3.3V15: no longer J16.4
- net 3.3V2: no longer J3.4
- net 3.3V3: no longer J4.4
- net 3.3V4: no longer J5.4
- net 3.3V5: no longer J6.4
- net 3.3V6: no longer J7.4
- net 3.3V7: no longer J8.4
- net 3.3V8: no longer J9.4
- net 3.3V9: no longer J10.4
- net N$101: now also TP78.P$1; no longer TP71.P$1
- net N$107: now also TP81.P$1; no longer TP74.P$1
- net N$108: now also TP82.P$1; no longer TP75.P$1
- net N$109: now also TP83.P$1; no longer TP76.P$1
- net N$115: now also TP89.P$1; no longer TP81.P$1
- net N$121: now also TP92.P$1; no longer TP84.P$1
- net N$122: now also TP93.P$1; no longer TP85.P$1
- net N$123: now also TP94.P$1; no longer TP86.P$1
- net N$129: now also TP100.P$1; no longer TP91.P$1
- net N$135: now also TP103.P$1; no longer TP94.P$1
- net N$136: now also TP104.P$1; no longer TP95.P$1
- net N$137: now also TP105.P$1; no longer TP96.P$1
- net N$143: now also TP111.P$1; no longer TP101.P$1
- net N$149: now also TP114.P$1; no longer TP104.P$1
- net N$150: now also TP115.P$1; no longer TP105.P$1
- net N$151: now also TP116.P$1; no longer TP106.P$1
- net N$157: now also TP122.P$1; no longer TP111.P$1
- net N$163: now also TP125.P$1; no longer TP114.P$1
- net N$164: now also TP126.P$1; no longer TP115.P$1
- net N$165: now also TP127.P$1; no longer TP116.P$1
- net N$171: now also TP133.P$1; no longer TP121.P$1
- net N$177: now also TP136.P$1; no longer TP124.P$1
- net N$178: now also TP137.P$1; no longer TP125.P$1
- net N$179: now also TP138.P$1; no longer TP126.P$1
- net N$18: now also TP15.P$1; no longer TP14.P$1
- net N$185: now also TP144.P$1; no longer TP131.P$1
- net N$19: now also TP16.P$1; no longer TP15.P$1
- net N$191: now also TP147.P$1; no longer TP134.P$1
- net N$192: now also TP148.P$1; no longer TP135.P$1
- net N$193: now also TP149.P$1; no longer TP136.P$1
- net N$199: now also TP155.P$1; no longer TP141.P$1
- net N$20: now also TP17.P$1; no longer TP16.P$1
- net N$205: now also TP158.P$1; no longer TP144.P$1
- net N$206: now also TP159.P$1; no longer TP145.P$1
- net N$207: now also TP160.P$1; no longer TP146.P$1
- net N$213: now also TP166.P$1; no longer TP151.P$1
- net N$219: now also TP169.P$1; no longer TP154.P$1
- net N$220: now also TP170.P$1; no longer TP155.P$1
- net N$221: now also TP171.P$1; no longer TP156.P$1
- net N$26: now also TP23.P$1; no longer TP21.P$1
- net N$37: now also TP26.P$1; no longer TP24.P$1
- net N$38: now also TP27.P$1; no longer TP25.P$1
- net N$39: now also TP28.P$1; no longer TP26.P$1
- net N$45: now also TP34.P$1; no longer TP31.P$1
- net N$51: now also TP37.P$1; no longer TP34.P$1
- net N$52: now also TP38.P$1; no longer TP35.P$1
- net N$53: now also TP39.P$1; no longer TP36.P$1
- net N$59: now also TP45.P$1; no longer TP41.P$1
- net N$65: now also TP48.P$1; no longer TP44.P$1
- net N$66: now also TP49.P$1; no longer TP45.P$1
- net N$67: now also TP50.P$1; no longer TP46.P$1
- net N$73: now also TP56.P$1; no longer TP51.P$1
- net N$79: now also TP59.P$1; no longer TP54.P$1
- net N$8: now also TP12.P$1; no longer TP2.P$1
- net N$80: now also TP60.P$1; no longer TP55.P$1
- net N$81: now also TP61.P$1; no longer TP56.P$1
- net N$87: now also TP67.P$1; no longer TP61.P$1
- net N$93: now also TP70.P$1; no longer TP64.P$1
- net N$94: now also TP71.P$1; no longer TP65.P$1
- net N$95: now also TP72.P$1; no longer TP66.P$1
- net PMIC: now also J1.4, TP2.P$1
- net PMIC1: now also J2.4, TP22.P$1
- net PMIC10: now also J11.4, TP121.P$1
- net PMIC11: now also J12.4, TP132.P$1
- net PMIC12: now also J13.4, TP143.P$1
- net PMIC13: now also J14.4, TP154.P$1
- net PMIC14: now also J15.4, TP165.P$1
- net PMIC15: now also J16.4, TP176.P$1
- net PMIC2: now also J3.4, TP33.P$1
- net PMIC3: now also J4.4, TP44.P$1
- net PMIC4: now also J5.4, TP55.P$1
- net PMIC5: now also J6.4, TP66.P$1
- net PMIC6: now also J7.4, TP77.P$1
- net PMIC7: now also J8.4, TP88.P$1
- net PMIC8: now also J9.4, TP99.P$1
- net PMIC9: now also J10.4, TP110.P$1
- net SWD_CLK1: now also TP19.P$1; no longer TP18.P$1
- net SWD_CLK10: now also TP118.P$1; no longer TP108.P$1
- net SWD_CLK11: now also TP129.P$1; no longer TP118.P$1
- net SWD_CLK12: now also TP140.P$1; no longer TP128.P$1
- net SWD_CLK13: now also TP151.P$1; no longer TP138.P$1
- net SWD_CLK14: now also TP162.P$1; no longer TP148.P$1
- net SWD_CLK15: now also TP173.P$1; no longer TP158.P$1
- net SWD_CLK2: now also TP30.P$1; no longer TP28.P$1
- net SWD_CLK3: now also TP41.P$1; no longer TP38.P$1
- net SWD_CLK4: now also TP52.P$1; no longer TP48.P$1
- net SWD_CLK5: now also TP63.P$1; no longer TP58.P$1
- net SWD_CLK6: now also TP74.P$1; no longer TP68.P$1
- net SWD_CLK7: now also TP85.P$1; no longer TP78.P$1
- net SWD_CLK8: now also TP96.P$1; no longer TP88.P$1
- net SWD_CLK9: now also TP107.P$1; no longer TP98.P$1
- net SWD_DIO1: now also TP18.P$1; no longer TP17.P$1
- net SWD_DIO10: now also TP117.P$1; no longer TP107.P$1
- net SWD_DIO11: now also TP128.P$1; no longer TP117.P$1
- net SWD_DIO12: now also TP139.P$1; no longer TP127.P$1
- net SWD_DIO13: now also TP150.P$1; no longer TP137.P$1
- net SWD_DIO14: now also TP161.P$1; no longer TP147.P$1
- net SWD_DIO15: now also TP172.P$1; no longer TP157.P$1
- net SWD_DIO2: now also TP29.P$1; no longer TP27.P$1
- net SWD_DIO3: now also TP40.P$1; no longer TP37.P$1
- net SWD_DIO4: now also TP51.P$1; no longer TP47.P$1
- net SWD_DIO5: now also TP62.P$1; no longer TP57.P$1
- net SWD_DIO6: now also TP73.P$1; no longer TP67.P$1
- net SWD_DIO7: now also TP84.P$1; no longer TP77.P$1
- net SWD_DIO8: now also TP95.P$1; no longer TP87.P$1
- net SWD_DIO9: now also TP106.P$1; no longer TP97.P$1
- net VCC1: now also TP13.P$1; no longer TP12.P$1
- net VCC10: now also TP112.P$1; no longer TP102.P$1
- net VCC11: now also TP123.P$1; no longer TP112.P$1
- net VCC12: now also TP134.P$1; no longer TP122.P$1
- net VCC13: now also TP145.P$1; no longer TP132.P$1
- net VCC14: now also TP156.P$1; no longer TP142.P$1
- net VCC15: now also TP167.P$1; no longer TP152.P$1
- net VCC2: now also TP24.P$1; no longer TP22.P$1
- net VCC3: now also TP35.P$1; no longer TP32.P$1
- net VCC4: now also TP46.P$1; no longer TP42.P$1
- net VCC5: now also TP57.P$1; no longer TP52.P$1
- net VCC6: now also TP68.P$1; no longer TP62.P$1
- net VCC7: now also TP79.P$1; no longer TP72.P$1
- net VCC8: now also TP90.P$1; no longer TP82.P$1
- net VCC9: now also TP101.P$1; no longer TP92.P$1
- net VDD_SOC_IN1: now also TP20.P$1; no longer TP19.P$1
- net VDD_SOC_IN10: now also TP119.P$1; no longer TP109.P$1
- net VDD_SOC_IN11: now also TP130.P$1; no longer TP119.P$1
- net VDD_SOC_IN12: now also TP141.P$1; no longer TP129.P$1
- net VDD_SOC_IN13: now also TP152.P$1; no longer TP139.P$1
- net VDD_SOC_IN14: now also TP163.P$1; no longer TP149.P$1
- net VDD_SOC_IN15: now also TP174.P$1; no longer TP159.P$1
- net VDD_SOC_IN2: now also TP31.P$1; no longer TP29.P$1
- net VDD_SOC_IN3: now also TP42.P$1; no longer TP39.P$1
- net VDD_SOC_IN4: now also TP53.P$1; no longer TP49.P$1
- net VDD_SOC_IN5: now also TP64.P$1; no longer TP59.P$1
- net VDD_SOC_IN6: now also TP75.P$1; no longer TP69.P$1
- net VDD_SOC_IN7: now also TP86.P$1; no longer TP79.P$1
- net VDD_SOC_IN8: now also TP97.P$1; no longer TP89.P$1
- net VDD_SOC_IN9: now also TP108.P$1; no longer TP99.P$1
- net VDD_USB_CAP1: now also TP21.P$1; no longer TP20.P$1
- net VDD_USB_CAP10: now also TP120.P$1; no longer TP110.P$1
- net VDD_USB_CAP11: now also TP131.P$1; no longer TP120.P$1
- net VDD_USB_CAP12: now also TP142.P$1; no longer TP130.P$1
- net VDD_USB_CAP13: now also TP153.P$1; no longer TP140.P$1
- net VDD_USB_CAP14: now also TP164.P$1; no longer TP150.P$1
- net VDD_USB_CAP15: now also TP175.P$1; no longer TP160.P$1
- net VDD_USB_CAP2: now also TP32.P$1; no longer TP30.P$1
- net VDD_USB_CAP3: now also TP43.P$1; no longer TP40.P$1
- net VDD_USB_CAP4: now also TP54.P$1; no longer TP50.P$1
- net VDD_USB_CAP5: now also TP65.P$1; no longer TP60.P$1
- net VDD_USB_CAP6: now also TP76.P$1; no longer TP70.P$1
- net VDD_USB_CAP7: now also TP87.P$1; no longer TP80.P$1
- net VDD_USB_CAP8: now also TP98.P$1; no longer TP90.P$1
- net VDD_USB_CAP9: now also TP109.P$1; no longer TP100.P$1
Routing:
- net PMIC7: track 1.20 -> 20.5 mm, vias 1 -> 2
- net PMIC6: track 1.20 -> 20.5 mm, vias 1 -> 2
- net PMIC14: track 1.20 -> 20.5 mm, vias 1 -> 2
- net PMIC2: track 1.20 -> 20.5 mm, vias 1 -> 2
- net PMIC3: track 1.20 -> 20.5 mm, vias 1 -> 2
- net PMIC: track 1.20 -> 20.5 mm, vias 1 -> 2
- net PMIC1: track 1.20 -> 20.5 mm, vias 1 -> 2
- net PMIC8: track 1.20 -> 20.5 mm, vias 1 -> 2
- net PMIC10: track 1.20 -> 20.5 mm, vias 1 -> 2
- net PMIC9: track 1.20 -> 20.5 mm, vias 1 -> 2
- net PMIC5: track 1.20 -> 20.5 mm, vias 1 -> 2
- net PMIC4: track 1.20 -> 20.5 mm, vias 1 -> 2
- net PMIC15: track 1.20 -> 20.5 mm, vias 1 -> 2
- net PMIC13: track 1.20 -> 20.5 mm, vias 1 -> 2
- net PMIC12: track 1.20 -> 20.5 mm, vias 1 -> 2
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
